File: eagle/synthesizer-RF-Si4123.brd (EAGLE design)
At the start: 45 x 38 mm, 47 parts, among them J1 142-0701-851, J2 142-0701-851, J3 142-0701-851, U1 LP38692, U2 SI4123, X1 ECS-TXO-3225

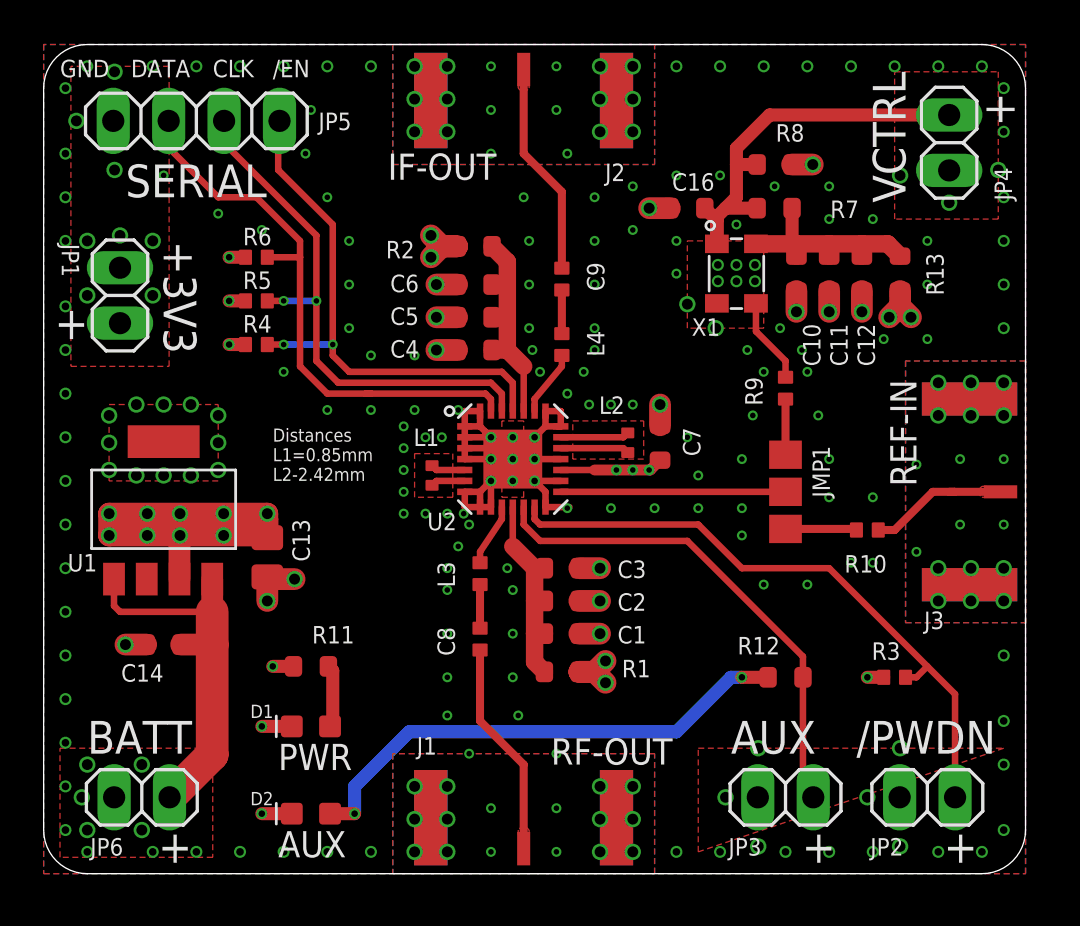
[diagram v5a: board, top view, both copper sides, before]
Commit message: Update SMA footprint
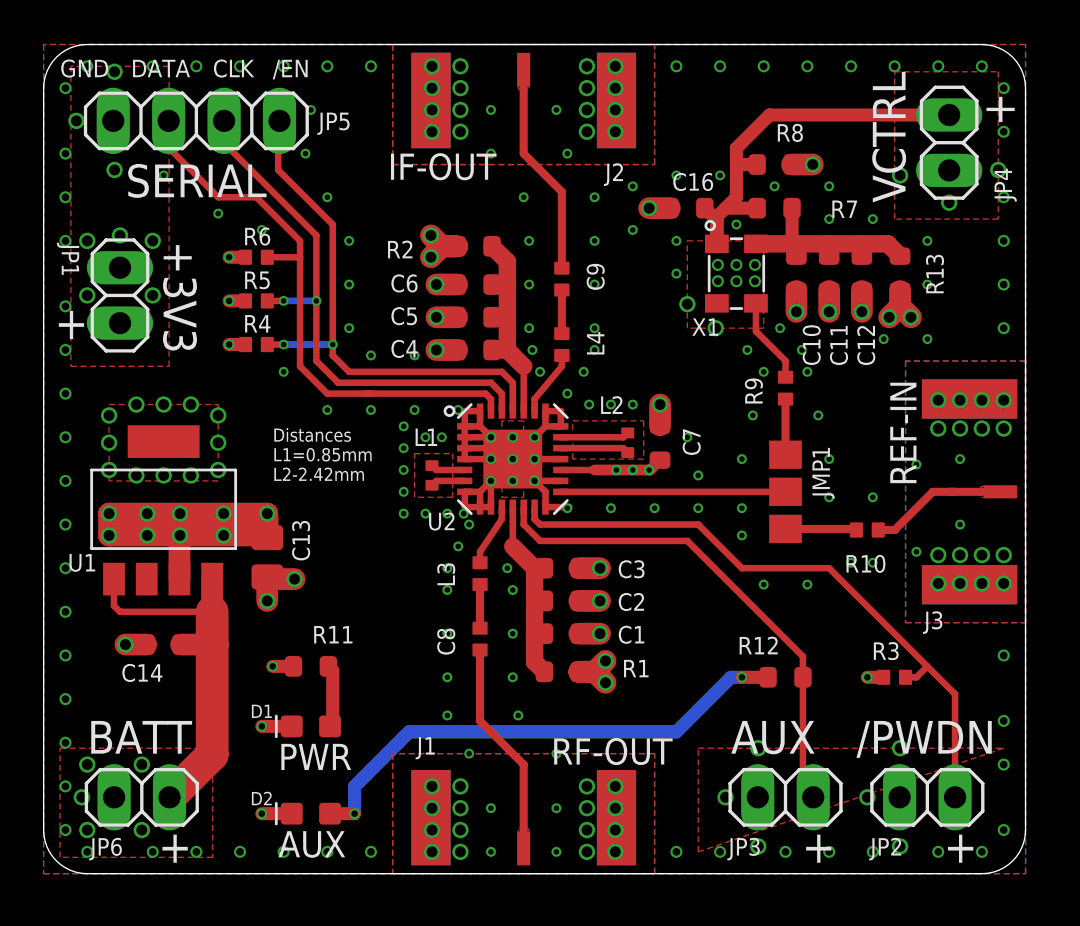
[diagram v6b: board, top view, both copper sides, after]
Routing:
- net GND: vias 270 -> 278
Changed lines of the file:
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@@
 <setting verticaltext="up"/>
 </settings>
-<grid distance="0.25" unitdist="mm" unit="mm" style="lines" multiple="4" display="yes" altdistance="0.01" altunitdist="mm" altunit="mm"/>
+<grid distance="0.1" unitdist="mm" unit="mm" style="lines" multiple="10" display="yes" altdistance="0.05" altunitdist="mm" altunit="mm"/>
 <layers>
 <layer number="1" name="Top" color="4" fill="1" visible="yes" active="yes"/>
@@
 <via x="29.5" y="20" extent="1-16" drill="0.254"/>
 <via x="37" y="14.25" extent="1-16" drill="0.254"/>
-<via x="44" y="16" extent="1-16" drill="0.254"/>
 <via x="42" y="16" extent="1-16" drill="0.254"/>
 <via x="40" y="14.75" extent="1-16" drill="0.254"/>
 <via x="38" y="14.25" extent="1-16" drill="0.254"/>
-<via x="44" y="14" extent="1-16" drill="0.5"/>
-<via x="42.5" y="14" extent="1-16" drill="0.5"/>
-<via x="41" y="14" extent="1-16" drill="0.5"/>
-<via x="41" y="12.5" extent="1-16" drill="0.5"/>
-<via x="42.5" y="12.5" extent="1-16" drill="0.5"/>
-<via x="44" y="12.5" extent="1-16" drill="0.5"/>
-<via x="41" y="21" extent="1-16" drill="0.5"/>
-<via x="42.5" y="21" extent="1-16" drill="0.5"/>
-<via x="44" y="21" extent="1-16" drill="0.5"/>
-<via x="44" y="22.5" extent="1-16" drill="0.5"/>
-<via x="42.5" y="22.5" extent="1-16" drill="0.5"/>
-<via x="41" y="22.5" extent="1-16" drill="0.5"/>
-<via x="44" y="19" extent="1-16" drill="0.254"/>
+<via x="43" y="14.6" extent="1-16" drill="0.5"/>
+<via x="42" y="14.6" extent="1-16" drill="0.5"/>
+<via x="41" y="14.6" extent="1-16" drill="0.5"/>
+<via x="41" y="13.3" extent="1-16" drill="0.5"/>
+<via x="42" y="13.3" extent="1-16" drill="0.5"/>
+<via x="43" y="13.3" extent="1-16" drill="0.5"/>
+<via x="42" y="20.4" extent="1-16" drill="0.5"/>
+<via x="43" y="20.4" extent="1-16" drill="0.5"/>
+<via x="44" y="20.4" extent="1-16" drill="0.5"/>
+<via x="44" y="21.7" extent="1-16" drill="0.5"/>
+<via x="43" y="21.7" extent="1-16" drill="0.5"/>
+<via x="41" y="20.4" extent="1-16" drill="0.5"/>
 <via x="42" y="19" extent="1-16" drill="0.254"/>
 <via x="40" y="18.75" extent="1-16" drill="0.254"/>
@@
 <via x="32.5" y="21" extent="1-16" drill="0.254"/>
 <via x="32" y="19" extent="1-16" drill="0.254"/>
-<via x="25.5" y="1" extent="1-16" drill="0.5"/>
-<via x="25.5" y="2.5" extent="1-16" drill="0.5"/>
-<via x="25.5" y="4" extent="1-16" drill="0.5"/>
-<via x="27" y="4" extent="1-16" drill="0.5"/>
-<via x="27" y="2.5" extent="1-16" drill="0.5"/>
-<via x="27" y="1" extent="1-16" drill="0.5"/>
-<via x="18.5" y="4" extent="1-16" drill="0.5"/>
-<via x="18.5" y="2.5" extent="1-16" drill="0.5"/>
-<via x="18.5" y="1" extent="1-16" drill="0.5"/>
-<via x="17" y="1" extent="1-16" drill="0.5"/>
-<via x="17" y="2.5" extent="1-16" drill="0.5"/>
-<via x="17" y="4" extent="1-16" drill="0.5"/>
-<via x="25.5" y="37" extent="1-16" drill="0.5"/>
-<via x="25.5" y="35.5" extent="1-16" drill="0.5"/>
-<via x="25.5" y="34" extent="1-16" drill="0.5"/>
-<via x="27" y="34" extent="1-16" drill="0.5"/>
-<via x="27" y="35.5" extent="1-16" drill="0.5"/>
-<via x="27" y="37" extent="1-16" drill="0.5"/>
-<via x="18.5" y="37" extent="1-16" drill="0.5"/>
-<via x="18.5" y="35.5" extent="1-16" drill="0.5"/>
-<via x="18.5" y="34" extent="1-16" drill="0.5"/>
-<via x="17" y="34" extent="1-16" drill="0.5"/>
-<via x="17" y="35.5" extent="1-16" drill="0.5"/>
-<via x="17" y="37" extent="1-16" drill="0.5"/>
-<via x="23.5" y="37" extent="1-16" drill="0.254"/>
-<via x="20.5" y="37" extent="1-16" drill="0.254"/>
+<via x="24.9" y="2" extent="1-16" drill="0.5"/>
+<via x="24.9" y="3" extent="1-16" drill="0.5"/>
+<via x="24.9" y="4" extent="1-16" drill="0.5"/>
+<via x="26.2" y="4" extent="1-16" drill="0.5"/>
+<via x="26.2" y="3" extent="1-16" drill="0.5"/>
+<via x="26.2" y="2" extent="1-16" drill="0.5"/>
+<via x="19.1" y="3" extent="1-16" drill="0.5"/>
+<via x="19.1" y="2" extent="1-16" drill="0.5"/>
+<via x="19.1" y="1" extent="1-16" drill="0.5"/>
+<via x="17.8" y="3" extent="1-16" drill="0.5"/>
+<via x="17.8" y="4" extent="1-16" drill="0.5"/>
+<via x="19.1" y="4" extent="1-16" drill="0.5"/>
+<via x="24.9" y="37" extent="1-16" drill="0.5"/>
+<via x="24.9" y="36" extent="1-16" drill="0.5"/>
+<via x="24.9" y="35" extent="1-16" drill="0.5"/>
+<via x="26.2" y="35" extent="1-16" drill="0.5"/>
+<via x="26.2" y="36" extent="1-16" drill="0.5"/>
+<via x="26.2" y="37" extent="1-16" drill="0.5"/>
+<via x="19.1" y="37" extent="1-16" drill="0.5"/>
+<via x="19.1" y="36" extent="1-16" drill="0.5"/>
+<via x="19.1" y="35" extent="1-16" drill="0.5"/>
+<via x="17.8" y="35" extent="1-16" drill="0.5"/>
+<via x="17.8" y="36" extent="1-16" drill="0.5"/>
+<via x="17.8" y="37" extent="1-16" drill="0.5"/>
 <via x="20.5" y="35" extent="1-16" drill="0.254"/>
 <via x="23.5" y="35" extent="1-16" drill="0.254"/>
@@
 <via x="2" y="5" extent="1-16" drill="0.5"/>
 <via x="2" y="2" extent="1-16" drill="0.5"/>
+<via x="17.8" y="34" extent="1-16" drill="0.5"/>
+<via x="19.1" y="34" extent="1-16" drill="0.5"/>
+<via x="24.9" y="34" extent="1-16" drill="0.5"/>
+<via x="26.2" y="34" extent="1-16" drill="0.5"/>
+<via x="44" y="14.6" extent="1-16" drill="0.5"/>
+<via x="44" y="13.3" extent="1-16" drill="0.5"/>
+<via x="41" y="21.7" extent="1-16" drill="0.5"/>
+<via x="42" y="21.7" extent="1-16" drill="0.5"/>
+<via x="24.9" y="1" extent="1-16" drill="0.5"/>
+<via x="26.2" y="1" extent="1-16" drill="0.5"/>
+<via x="17.8" y="2" extent="1-16" drill="0.5"/>
+<via x="17.8" y="1" extent="1-16" drill="0.5"/>
 </signal>
 <signal name="N$5">
